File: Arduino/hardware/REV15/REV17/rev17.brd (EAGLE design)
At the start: 50 x 50 mm, 9 parts

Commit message: up to rev18 cleaned up
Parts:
- moved U$2 28.0 mm to (-7.75, 25.8)
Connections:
- removed net N$20: RFM22B.3, RFM22B.6
- removed net N$21: RFM22B.4, RFM22B.7
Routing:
- net N$21: track 8.57 -> 0.00 mm
- net N$20: track 7.34 -> 0.00 mm
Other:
- board text removed: "Remove jumper if battery power"
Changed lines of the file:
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@@
 <plain>
 <text x="-5.318971875" y="13.33876875" size="1" layer="25" font="vector" rot="R180">20151208</text>
-<text x="24.149196875" y="-4.224378125" size="1" layer="22" font="vector" rot="MR0">License: http://goo.gl/3d71UJ</text>
-<text x="12.333878125" y="-0.70546875" size="1" layer="25" font="vector" rot="R180">OpenTRV.org.uk</text>
-<text x="-8.89" y="40.64" size="1" layer="25" rot="R270">Remove jumper
-if battery power</text>
+<text x="36.849196875" y="0.855621875" size="1" layer="22" font="vector" rot="MR0">License: http://goo.gl/3d71UJ</text>
+<text x="31.383878125" y="1.83453125" size="1" layer="25" font="vector" rot="R180">OpenTRV.org.uk</text>
 <wire x1="0" y1="0" x2="0" y2="50" width="0.4064" layer="20"/>
 <wire x1="0" y1="50" x2="50" y2="50" width="0.4064" layer="20"/>
@@
 </autorouter>
 <elements>
-<element name="U$2" library="logo" package="TONNE" value="" x="-9.025" y="53.75711875"/>
+<element name="U$2" library="logo" package="TONNE" value="" x="-7.755" y="25.81711875"/>
 <element name="U$1" library="ohw-logo" package="OSHW_10X200_NOTEXT" value="" x="-10.725834375" y="16.02610625"/>
 <element name="I2C_EXT" library="pinhead" package="2X10" value="" x="18.05" y="45.905" smashed="yes">
@@
 <signal name="N$29">
 </signal>
-<signal name="N$20">
-<contactref element="RFM22B" pad="3"/>
-<contactref element="RFM22B" pad="6"/>
-<wire x1="41.2496" y1="22.4536" x2="41.0464" y2="22.4536" width="0.2032" layer="1"/>
-<wire x1="42.3672" y1="23.5712" x2="41.2496" y2="22.4536" width="0.2032" layer="1"/>
-<wire x1="42.3672" y1="27.2288" x2="42.3672" y2="23.5712" width="0.2032" layer="1"/>
-<wire x1="41.2496" y1="28.3464" x2="42.3672" y2="27.2288" width="0.2032" layer="1"/>
-<wire x1="41.0464" y1="28.3464" x2="41.2496" y2="28.3464" width="0.2032" layer="1"/>
-<wire x1="41.0464" y1="22.4536" x2="41.02" y2="22.4" width="0.2032" layer="1"/>
-<wire x1="41.0464" y1="28.3464" x2="41.02" y2="28.4" width="0.2032" layer="1"/>
-</signal>
-<signal name="N$21">
-<contactref element="RFM22B" pad="4"/>
-<contactref element="RFM22B" pad="7"/>
-<wire x1="40.2336" y1="24.4856" x2="40.9448" y2="24.4856" width="0.2032" layer="1"/>
-<wire x1="38.608" y1="26.1112" x2="40.2336" y2="24.4856" width="0.2032" layer="1"/>
-<wire x1="38.608" y1="28.1432" x2="38.608" y2="26.1112" width="0.2032" layer="1"/>
-<wire x1="40.9448" y1="30.48" x2="38.608" y2="28.1432" width="0.2032" layer="1"/>
-<wire x1="40.9448" y1="24.4856" x2="41.02" y2="24.4" width="0.2032" layer="1"/>
-<wire x1="40.9448" y1="30.48" x2="41.02" y2="30.4" width="0.2032" layer="1"/>
-</signal>
 <signal name="N$26" class="2">
 <contactref element="ANT" pad="1"/>
@@
 </board>
 </drawing>
-<compatibility>
-<note version="6.3" minversion="6.2.2" severity="warning">
-Since Version 6.2.2 text objects can contain more than one line,
-which will not be processed correctly with this version.
-</note>
-</compatibility>
 </eagle>

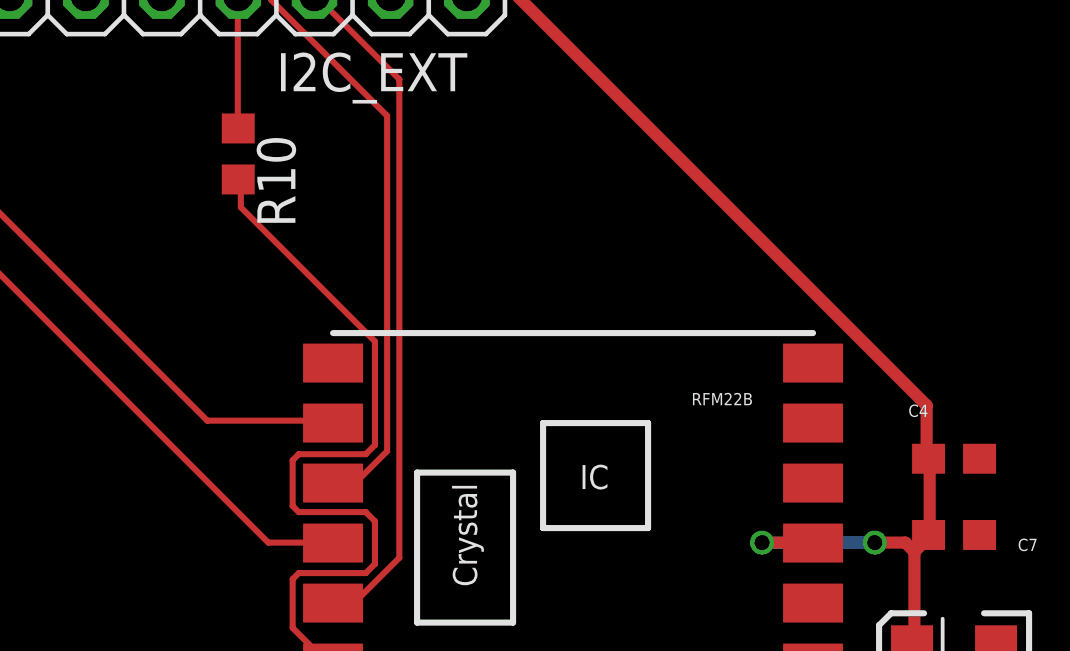
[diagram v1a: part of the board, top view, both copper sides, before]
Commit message: up to rev18 DRC check and ground plane
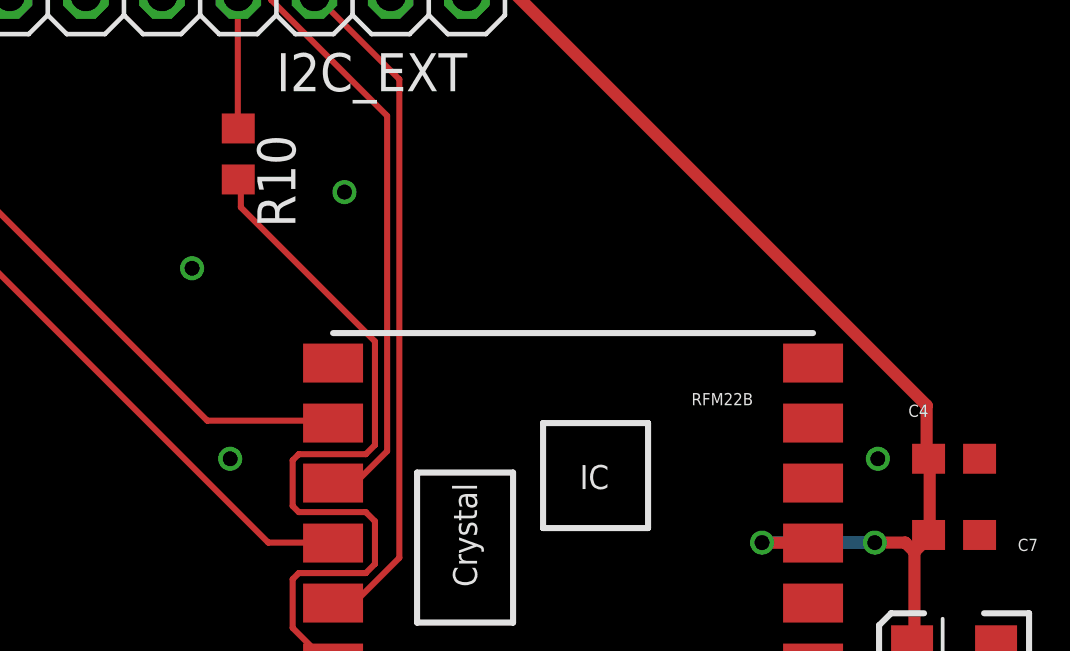
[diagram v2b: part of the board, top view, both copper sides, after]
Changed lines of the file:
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@@
 <contactref element="C7" pad="1"/>
 <contactref element="RFM22B" pad="15"/>
-<wire x1="25.02" y1="32.4" x2="25.02" y2="20.4" width="0" layer="19" extent="1-1"/>
+<via x="25.4" y="38.1" extent="1-16" drill="0.5"/>
+<via x="21.59" y="29.21" extent="1-16" drill="0.5"/>
+<via x="20.32" y="35.56" extent="1-16" drill="0.5"/>
+<via x="43.18" y="29.21" extent="1-16" drill="0.5"/>
 </signal>
 <signal name="32KHZ">

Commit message: REV15-18 cleaned up, need sanity check
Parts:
- moved U$1 35.8 mm to (23.6, 5.87)
- moved U$2 18.9 mm to (10.0, 19.5)
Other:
- board text added: "20160229"
- board text removed: "20151208"
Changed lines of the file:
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@@
 <board>
 <plain>
-<text x="-5.318971875" y="13.33876875" size="1" layer="25" font="vector" rot="R180">20151208</text>
+<text x="47.62123125" y="13.731028125" size="1" layer="25" font="vector" rot="R270">20160229</text>
 <text x="36.849196875" y="0.855621875" size="1" layer="22" font="vector" rot="MR0">License: http://goo.gl/3d71UJ</text>
 <text x="31.383878125" y="1.83453125" size="1" layer="25" font="vector" rot="R180">OpenTRV.org.uk</text>
@@
 </autorouter>
 <elements>
-<element name="U$2" library="logo" package="TONNE" value="" x="-7.755" y="25.81711875"/>
-<element name="U$1" library="ohw-logo" package="OSHW_10X200_NOTEXT" value="" x="-10.725834375" y="16.02610625"/>
+<element name="U$2" library="logo" package="TONNE" value="" x="10.025" y="19.46711875"/>
+<element name="U$1" library="ohw-logo" package="OSHW_10X200_NOTEXT" value="" x="23.564165625" y="5.86610625"/>
 <element name="I2C_EXT" library="pinhead" package="2X10" value="" x="18.05" y="45.905" smashed="yes">
 <attribute name="NAME" x="23.13" y="41.46" size="1.27" layer="25" ratio="10"/>

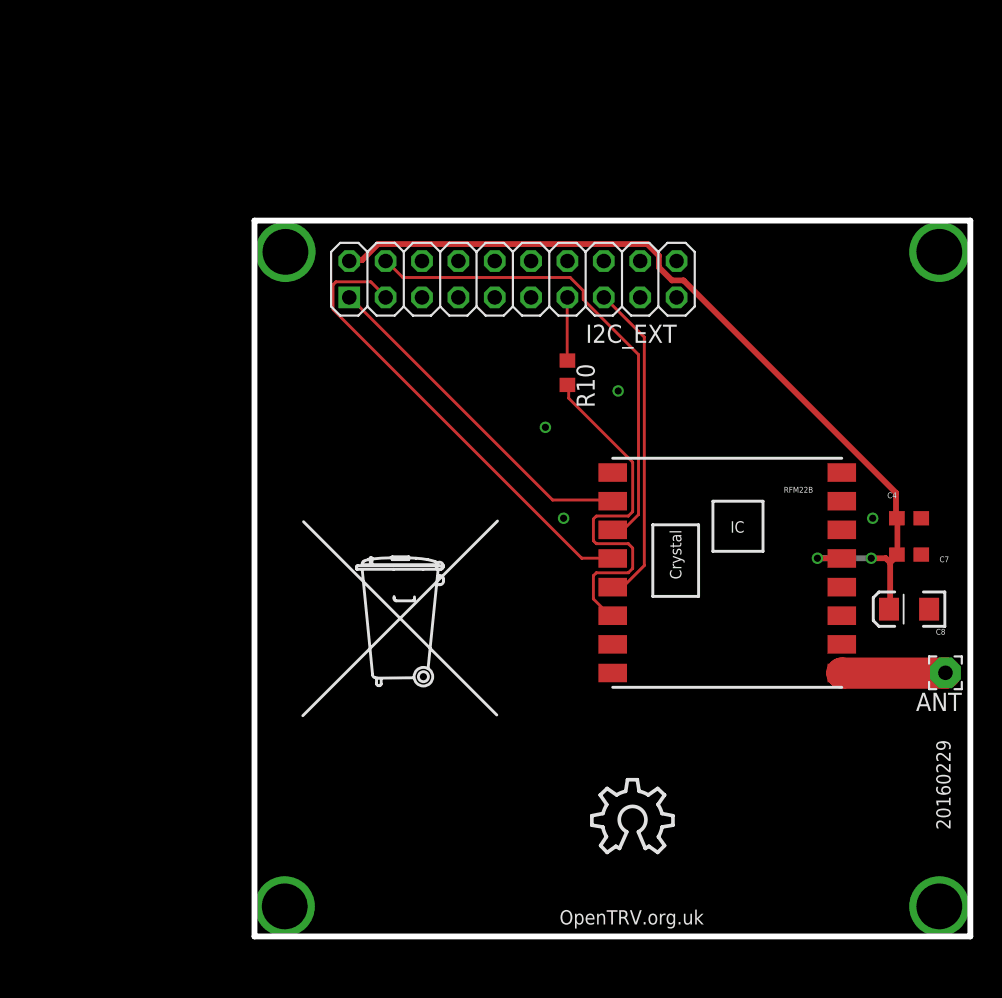
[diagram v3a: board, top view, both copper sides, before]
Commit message: rev15-18 changed as per Deniz suggeastions
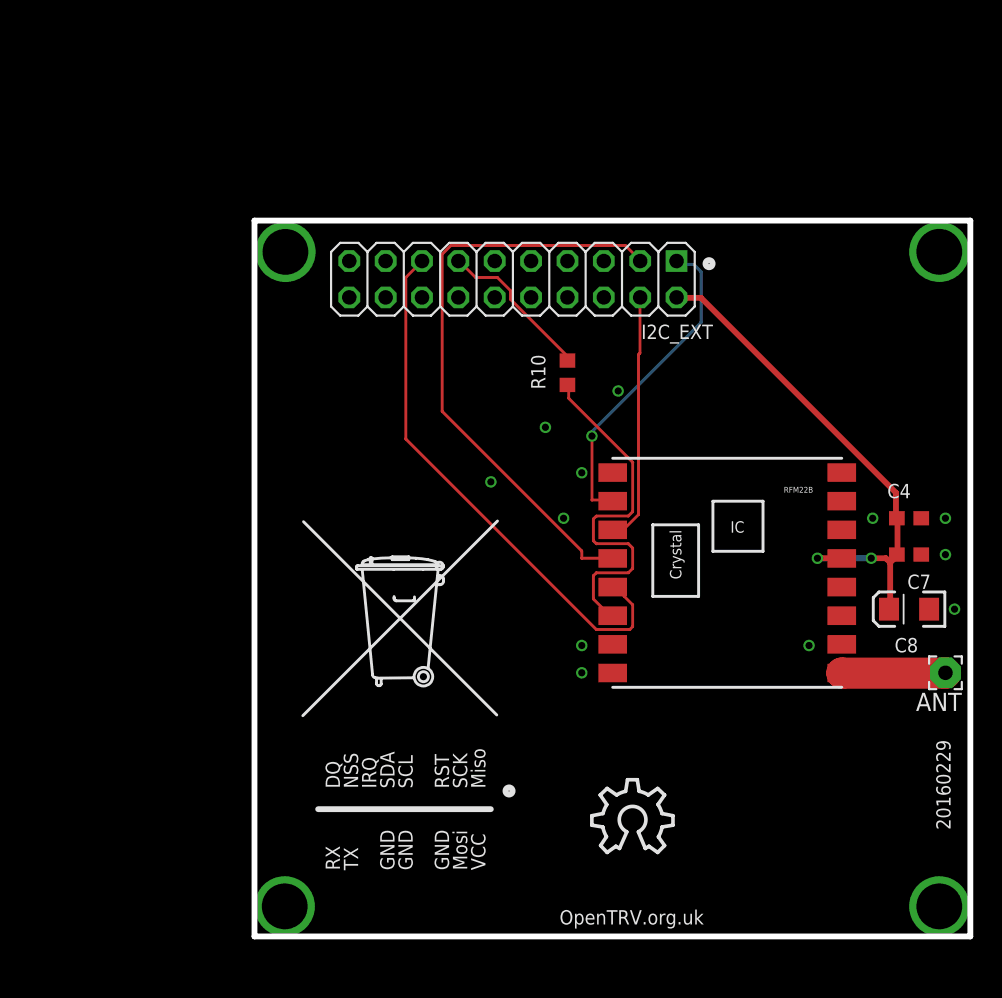
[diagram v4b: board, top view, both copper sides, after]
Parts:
- turned I2C_EXT to 180 degrees
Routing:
- net VCC: track 61.7 -> 36.3 mm
- net SPI_MOSI: track 34.1 -> 17.5 mm
- net SPI_NSS: track 22.8 -> 39.1 mm
- net SPI_SCK: track 32.7 -> 42.0 mm
- net RFM_IRQ: track 4.43 -> 11.0 mm
- net SPI_MISO: track 24.3 -> 22.6 mm, vias 0 -> 1
- net GND: track 0.00 -> 0.19 mm, vias 8 -> 16
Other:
- board text added: "DQ"
- board text added: "GND"
- board text added: "IRQ"
- board text added: "Miso"
- board text added: "Mosi"
- board text added: "NSS"
- board text added: "RST"
- board text added: "RX"
- board text added: "SCK"
- board text added: "SCL"
- board text added: "SDA"
- board text added: "TX"
- board text added: "VCC"

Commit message: ic2_ext labels closer to connector
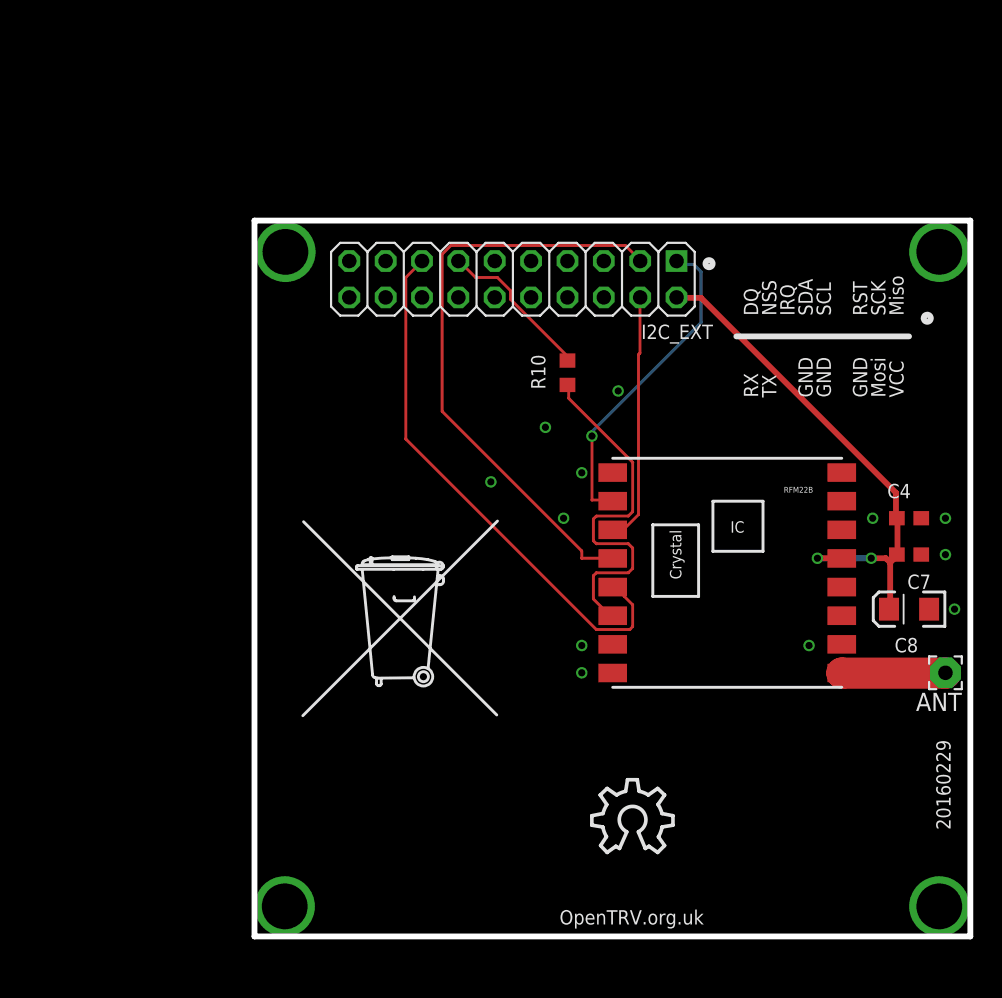
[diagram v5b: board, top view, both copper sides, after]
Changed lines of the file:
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@@
 <wire x1="50" y1="50" x2="50" y2="0" width="0.4064" layer="20"/>
 <wire x1="50" y1="0" x2="0" y2="0" width="0.4064" layer="20"/>
-<text x="5.97" y="10.34" size="1" layer="25" rot="R90">DQ</text>
-<text x="9.78" y="10.34" size="1" layer="25" rot="R90">SDA</text>
-<text x="16.13" y="10.34" size="1" layer="25" rot="R90">Miso</text>
-<text x="16.13" y="4.625" size="1" layer="25" rot="R90">VCC</text>
-<text x="14.86" y="10.34" size="1" layer="25" rot="R90">SCK</text>
-<text x="14.86" y="4.625" size="1" layer="25" rot="R90">Mosi</text>
-<text x="13.59" y="10.34" size="1" layer="25" rot="R90">RST</text>
-<text x="13.59" y="4.625" size="1" layer="25" rot="R90">GND</text>
-<text x="8.51" y="10.34" size="1" layer="25" rot="R90">IRQ</text>
-<text x="7.24" y="10.34" size="1" layer="25" rot="R90">NSS</text>
-<text x="5.97" y="4.625" size="1" layer="25" rot="R90">RX</text>
-<text x="11.05" y="10.34" size="1" layer="25" rot="R90">SCL</text>
-<text x="7.24" y="4.625" size="1" layer="25" rot="R90">TX</text>
-<wire x1="16.51" y1="8.89" x2="4.445" y2="8.89" width="0.4064" layer="25"/>
-<text x="11.05" y="4.625" size="1" layer="25" rot="R90">GND</text>
-<text x="9.78" y="4.625" size="1" layer="25" rot="R90">GND</text>
-<circle x="17.78" y="10.16" radius="0.25" width="0.4064" layer="25"/>
+<text x="35.18" y="43.36" size="1" layer="25" rot="R90">DQ</text>
+<text x="38.99" y="43.36" size="1" layer="25" rot="R90">SDA</text>
+<text x="45.34" y="43.36" size="1" layer="25" rot="R90">Miso</text>
+<text x="45.34" y="37.645" size="1" layer="25" rot="R90">VCC</text>
+<text x="44.07" y="43.36" size="1" layer="25" rot="R90">SCK</text>
+<text x="44.07" y="37.645" size="1" layer="25" rot="R90">Mosi</text>
+<text x="42.8" y="43.36" size="1" layer="25" rot="R90">RST</text>
+<text x="42.8" y="37.645" size="1" layer="25" rot="R90">GND</text>
+<text x="37.72" y="43.36" size="1" layer="25" rot="R90">IRQ</text>
+<text x="36.45" y="43.36" size="1" layer="25" rot="R90">NSS</text>
+<text x="35.18" y="37.645" size="1" layer="25" rot="R90">RX</text>
+<text x="40.26" y="43.36" size="1" layer="25" rot="R90">SCL</text>
+<text x="36.45" y="37.645" size="1" layer="25" rot="R90">TX</text>
+<wire x1="45.72" y1="41.91" x2="33.655" y2="41.91" width="0.4064" layer="25"/>
+<text x="40.26" y="37.645" size="1" layer="25" rot="R90">GND</text>
+<text x="38.99" y="37.645" size="1" layer="25" rot="R90">GND</text>
+<circle x="46.99" y="43.18" radius="0.25" width="0.4064" layer="25"/>
 <circle x="31.75" y="46.99" radius="0.25" width="0.4064" layer="25"/>
 </plain>
